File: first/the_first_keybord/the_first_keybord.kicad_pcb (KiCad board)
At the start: 2 copper layers, 1 part, among them U1 ATmega32U4-A

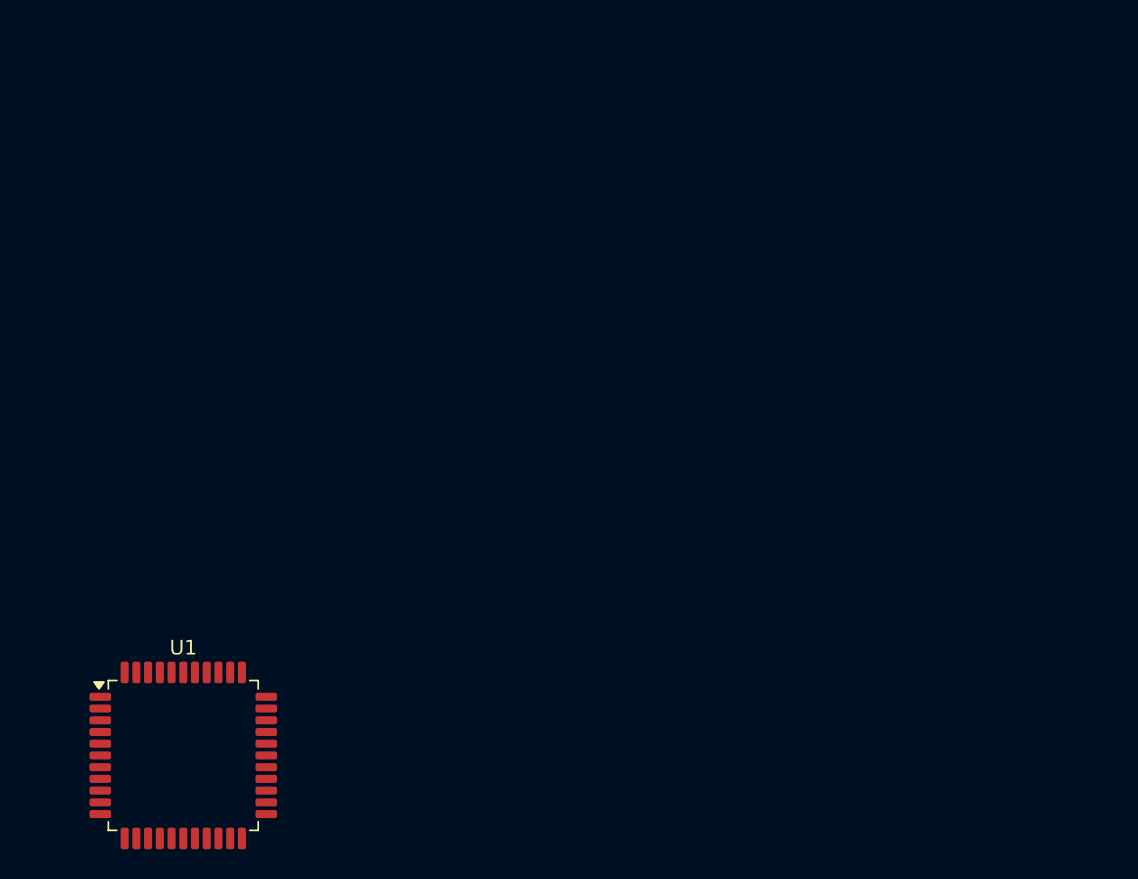
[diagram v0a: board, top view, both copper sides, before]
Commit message: add keyboard
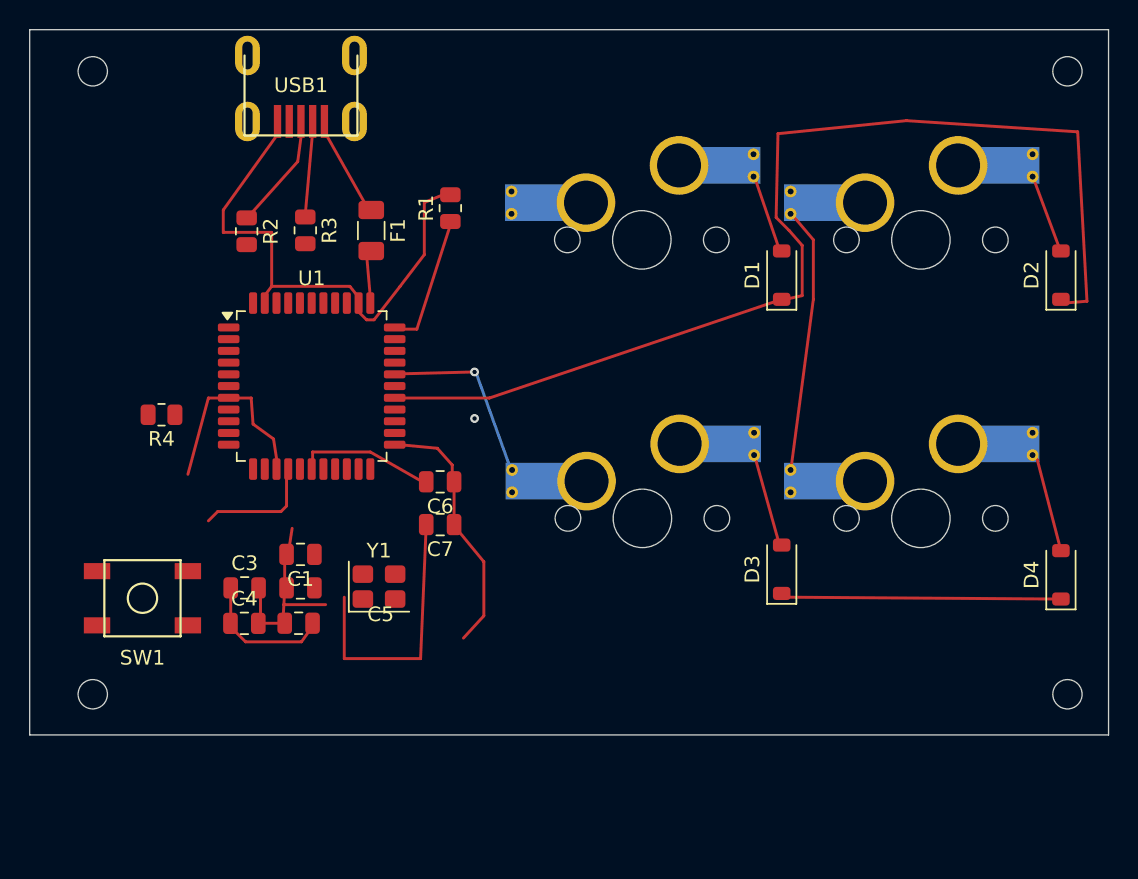
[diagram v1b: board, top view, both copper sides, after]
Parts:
- added C1: C_Small, Capacitor_SMD:C_0805_2012Metric, F.Cu at (126.2, 100.5)
- added C2: C_Small, Capacitor_SMD:C_0805_2012Metric, F.Cu at (126.2, 102.7)
- added C3: C_Small, Capacitor_SMD:C_0805_2012Metric, F.Cu at (122.4, 102.7)
- added C4: C_Small, Capacitor_SMD:C_0805_2012Metric, F.Cu at (122.3, 105.2)
- added C5: C_Small, Capacitor_SMD:C_0805_2012Metric, F.Cu at (126.0, 105.2)
- added C6: C_Small, Capacitor_SMD:C_0805_2012Metric, F.Cu at (135.7, 95.5)
- added C7: C_Small, Capacitor_SMD:C_0805_2012Metric, F.Cu at (135.7, 98.4)
- added D1: D, Diode_SMD:D_SOD-123, F.Cu at (159.0, 81.4)
- added D2: D, Diode_SMD:D_SOD-123, F.Cu at (178.1, 81.4)
- added D3: D, Diode_SMD:D_SOD-123, F.Cu at (159.0, 101.5)
- added D4: D, Diode_SMD:D_SOD-123, F.Cu at (178.1, 101.9)
- added F1: 500mA, Fuse:Fuse_1206_3216Metric, F.Cu at (131.0, 78.4)
- added MX1: MX-NoLED, MX_Only:MXOnly-1U-Hotswap-Antishear, F.Cu at (149.5, 79.0)
- added MX2: MX-NoLED, MX_Only:MXOnly-1U-Hotswap-Antishear, F.Cu at (168.5, 79.0)
- added MX3: MX-NoLED, MX_Only:MXOnly-1U-Hotswap-Antishear, F.Cu at (149.5, 98.0)
- added MX4: MX-NoLED, MX_Only:MXOnly-1U-Hotswap-Antishear, F.Cu at (168.5, 98.0)
- added R1: R_Small, Resistor_SMD:R_0805_2012Metric, F.Cu at (136.4, 76.8)
- added R2: R_Small, Resistor_SMD:R_0805_2012Metric, F.Cu at (122.5, 78.4)
- added R3: R_Small, Resistor_SMD:R_0805_2012Metric, F.Cu at (126.5, 78.3)
- added R4: R, Resistor_SMD:R_0805_2012Metric, F.Cu at (116.7, 90.9)
- added SW1: SW_Push, random-keyboard-parts:SKQG-1155865, F.Cu at (115.4, 103.5)
- added USB1: Molex-0548190589, random-keyboard-parts:Molex-0548190589, F.Cu at (126.2, 66.4)
- added Y1: Crystal_GND24_Small, Crystal:Crystal_SMD_3225-4Pin_3.2x2.5mm, F.Cu at (131.5, 102.7)
- moved U1 26.7 mm to (126.9, 89.0)
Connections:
- U1 pad 27: unconnected-(U1-PD7-Pad27) -> ROW0
- U1 pad 28: unconnected-(U1-PB4-Pad28) -> COL1
- U1 pad 29: unconnected-(U1-PB5-Pad29) -> COL0
- U1 pad 30: unconnected-(U1-PB6-Pad30) -> ROW1
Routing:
- net COL0: vias 0 -> 1
- net (no net): vias 0 -> 1
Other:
- board outline added: 73.6 x 48.1 mm
